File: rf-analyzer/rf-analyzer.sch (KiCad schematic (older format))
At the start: 50 parts, among them U1 AD8302, U2 AD8302, U3 OPA695

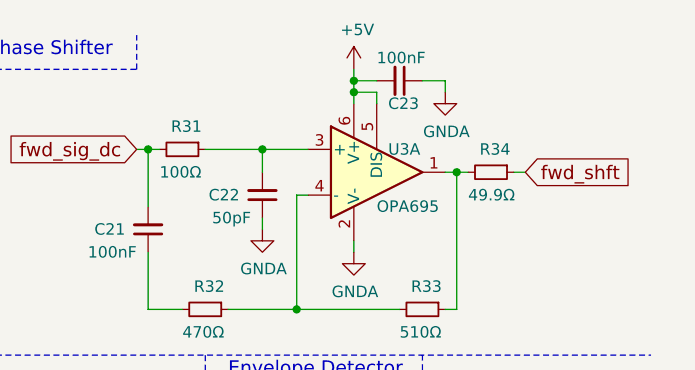
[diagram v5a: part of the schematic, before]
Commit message: Minor tweak to make phase shifter fit in the schematic.
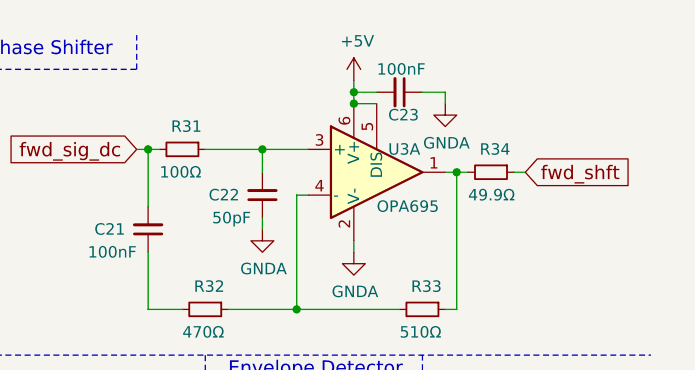
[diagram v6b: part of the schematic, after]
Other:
- moved on the sheet: C23
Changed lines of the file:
@@
 L Device:C_Small C23
 U 1 1 596FF084
-P 10100 700
-F 0 "C23" V 10200 650 50  0000 L CNN
-F 1 "100nF" V 10000 600 50  0000 L CNN
-F 2 "Capacitor_SMD:C_0603_1608Metric_Pad1.05x0.95mm_HandSolder" H 10100 700 50  0001 C CNN
-F 3 "" H 10100 700 50  0001 C CNN
-	1    10100 700
+P 10100 750
+F 0 "C23" V 10200 700 50  0000 L CNN
+F 1 "100nF" V 10000 650 50  0000 L CNN
+F 2 "Capacitor_SMD:C_0603_1608Metric_Pad1.05x0.95mm_HandSolder" H 10100 750 50  0001 C CNN
+F 3 "" H 10100 750 50  0001 C CNN
+	1    10100 750
 	0    1    1    0
 $EndComp
@@
 fwd_sig
 Wire Wire Line
-	9900 650  9900 700
-Wire Wire Line
-	10000 800  10000 750
+	9900 700  9900 750
+Wire Wire Line
+	10000 800  9900 800
 Wire Wire Line
 	10000 750  9900 750
 Connection ~ 9900 750
 Wire Wire Line
-	10000 700  9900 700
-Connection ~ 9900 700
-Wire Wire Line
-	10200 700  10300 700
-Wire Wire Line
-	10300 700  10300 750
+	10200 750  10300 750
+Wire Wire Line
+	10300 750  10300 800
 Wire Wire Line
 	10300 1700 10350 1700
@@
 	9900 750  9900 800
 Wire Wire Line
-	9900 700  9900 750
-Wire Wire Line
 	9650 1700 10100 1700
 Wire Wire Line
@@
 L power:GNDA #PWR0123
 U 1 1 5C553890
-P 10300 750
-F 0 "#PWR0123" H 10300 500 50  0001 C CNN
-F 1 "GNDA" H 10305 577 50  0000 C CNN
-F 2 "" H 10300 750 50  0001 C CNN
-F 3 "" H 10300 750 50  0001 C CNN
-	1    10300 750
+P 10300 800
+F 0 "#PWR0123" H 10300 550 50  0001 C CNN
+F 1 "GNDA" H 10305 627 50  0000 C CNN
+F 2 "" H 10300 800 50  0001 C CNN
+F 3 "" H 10300 800 50  0001 C CNN
+	1    10300 800
 	1    0    0    -1
 $EndComp
@@
 L power:+5V #PWR0105
 U 1 1 5C5E9076
-P 9900 650
-F 0 "#PWR0105" H 9900 500 50  0001 C CNN
-F 1 "+5V" H 9915 823 50  0000 C CNN
-F 2 "" H 9900 650 50  0001 C CNN
-F 3 "" H 9900 650 50  0001 C CNN
-	1    9900 650
+P 9900 700
+F 0 "#PWR0105" H 9900 550 50  0001 C CNN
+F 1 "+5V" H 9915 873 50  0000 C CNN
+F 2 "" H 9900 700 50  0001 C CNN
+F 3 "" H 9900 700 50  0001 C CNN
+	1    9900 700
 	1    0    0    -1
 $EndComp
@@
 Wire Notes Line
 	9950 3950 8650 3950
+Connection ~ 9900 800
 $EndSCHEMATC

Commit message: Associated correct footprint with Due shield in schematic.
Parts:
- XA?: footprint (none) -> Arduino:Arduino_Due_Shield
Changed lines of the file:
@@
 F 0 "XA?" H 2500 5300 60  0000 C CNN
 F 1 "Arduino_Due_Shield" H 2500 5450 60  0000 C CNN
-F 2 "" H 3200 8050 60  0001 C CNN
+F 2 "Arduino:Arduino_Due_Shield" H 3200 8050 60  0001 C CNN
 F 3 "https://store.arduino.cc/arduino-due" H 3200 8050 60  0001 C CNN
 	1    2500 5300

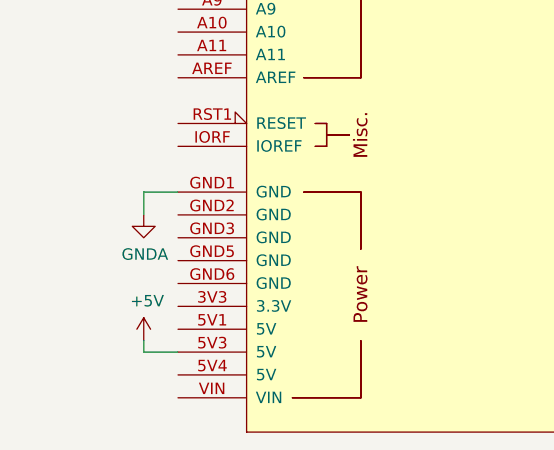
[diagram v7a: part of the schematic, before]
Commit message: Fixed powerrails to use all pins on Due shield.
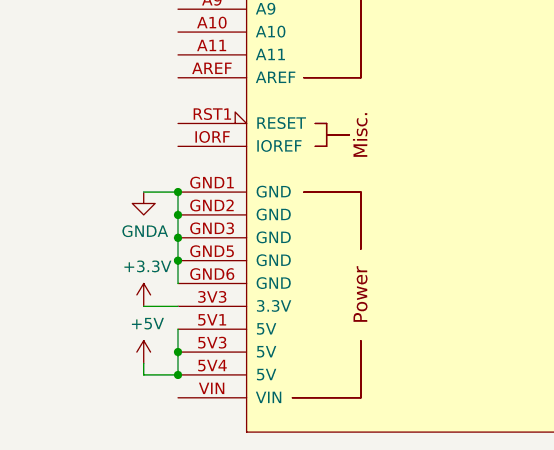
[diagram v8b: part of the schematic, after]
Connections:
- net +3V3: now also XA?.3V3 (3.3V)
- net +5V: now also XA?.5V1 (5V), XA?.5V4 (5V)
- net GNDA: now also XA?.GND2 (GND), XA?.GND3 (GND), XA?.GND5 (GND), XA?.GND6 (GND)
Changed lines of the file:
@@
 L power:+5V #PWR0129
 U 1 1 5C60E1CE
-P 1050 7200
-F 0 "#PWR0129" H 1050 7050 50  0001 C CNN
-F 1 "+5V" H 1065 7373 50  0000 C CNN
-F 2 "" H 1050 7200 50  0001 C CNN
-F 3 "" H 1050 7200 50  0001 C CNN
-	1    1050 7200
+P 1050 7300
+F 0 "#PWR0129" H 1050 7150 50  0001 C CNN
+F 1 "+5V" H 1065 7473 50  0000 C CNN
+F 2 "" H 1050 7300 50  0001 C CNN
+F 3 "" H 1050 7300 50  0001 C CNN
+	1    1050 7300
 	1    0    0    -1
 $EndComp
@@
 L power:GNDA #PWR0130
 U 1 1 5C62106F
-P 1050 6650
-F 0 "#PWR0130" H 1050 6400 50  0001 C CNN
-F 1 "GNDA" H 1055 6477 50  0000 C CNN
-F 2 "" H 1050 6650 50  0001 C CNN
-F 3 "" H 1050 6650 50  0001 C CNN
-	1    1050 6650
+P 1050 6550
+F 0 "#PWR0130" H 1050 6300 50  0001 C CNN
+F 1 "GNDA" H 1055 6377 50  0000 C CNN
+F 2 "" H 1050 6550 50  0001 C CNN
+F 3 "" H 1050 6550 50  0001 C CNN
+	1    1050 6550
 	1    0    0    -1
 $EndComp
@@
 	1200 6550 1050 6550
 Wire Wire Line
-	1050 6550 1050 6650
-Wire Wire Line
-	1050 7200 1050 7250
-Wire Wire Line
-	1050 7250 1200 7250
+	1050 7300 1050 7350
+Wire Wire Line
+	1050 7350 1200 7350
 Text GLabel 1050 4300 0    50   Input ~ 0
 SCL
@@
 	9950 3950 8650 3950
 Connection ~ 9900 800
+$Comp
+L power:+3.3V #PWR?
+U 1 1 60417FFB
+P 1050 7050
+F 0 "#PWR?" H 1050 6900 50  0001 C CNN
+F 1 "+3.3V" H 1065 7223 50  0000 C CNN
+F 2 "" H 1050 7050 50  0001 C CNN
+F 3 "" H 1050 7050 50  0001 C CNN
+	1    1050 7050
+	1    0    0    -1
+$EndComp
+Wire Wire Line
+	1050 7050 1200 7050
+Wire Wire Line
+	1200 6950 1200 6850
+Wire Wire Line
+	1200 6850 1200 6750
+Connection ~ 1200 6850
+Wire Wire Line
+	1200 6750 1200 6650
+Connection ~ 1200 6750
+Wire Wire Line
+	1200 6650 1200 6550
+Connection ~ 1200 6650
+Connection ~ 1200 6550
+Wire Wire Line
+	1200 7350 1200 7250
+Connection ~ 1200 7350
+Wire Wire Line
+	1200 7250 1200 7150
+Connection ~ 1200 7250
 $EndSCHEMATC
